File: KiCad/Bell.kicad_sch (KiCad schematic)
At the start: 34 parts, among them J1 USB-C, J2 POWER, J3 Conn_01x10, U1 ESP32-WROOM-32, U2 FT231XQ, U3 ISL89410, U4 ISL89410, U5 LMR16006+FB, U6 AA, U7 QR

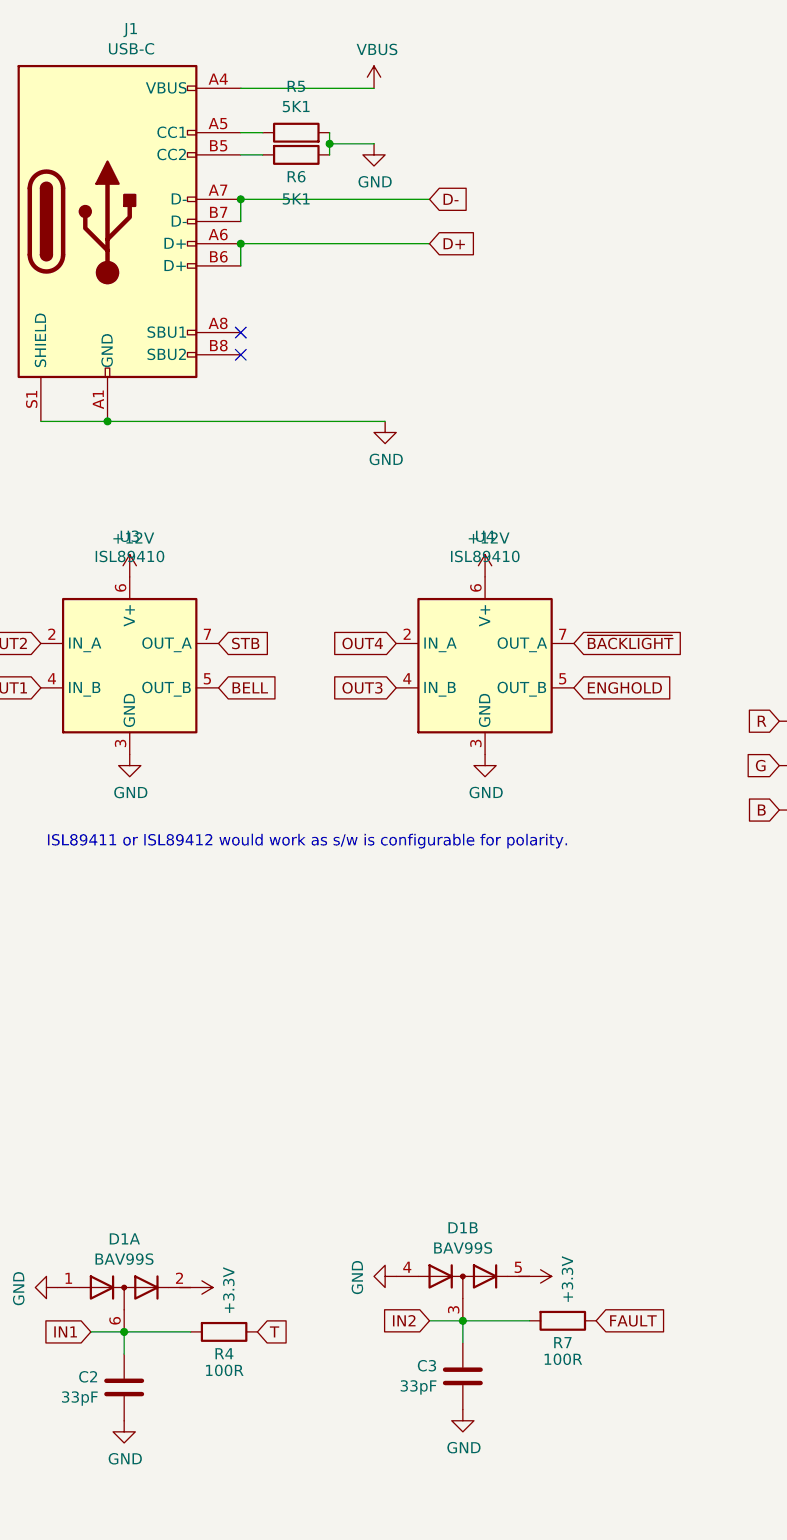
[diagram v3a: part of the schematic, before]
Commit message: VBUS update
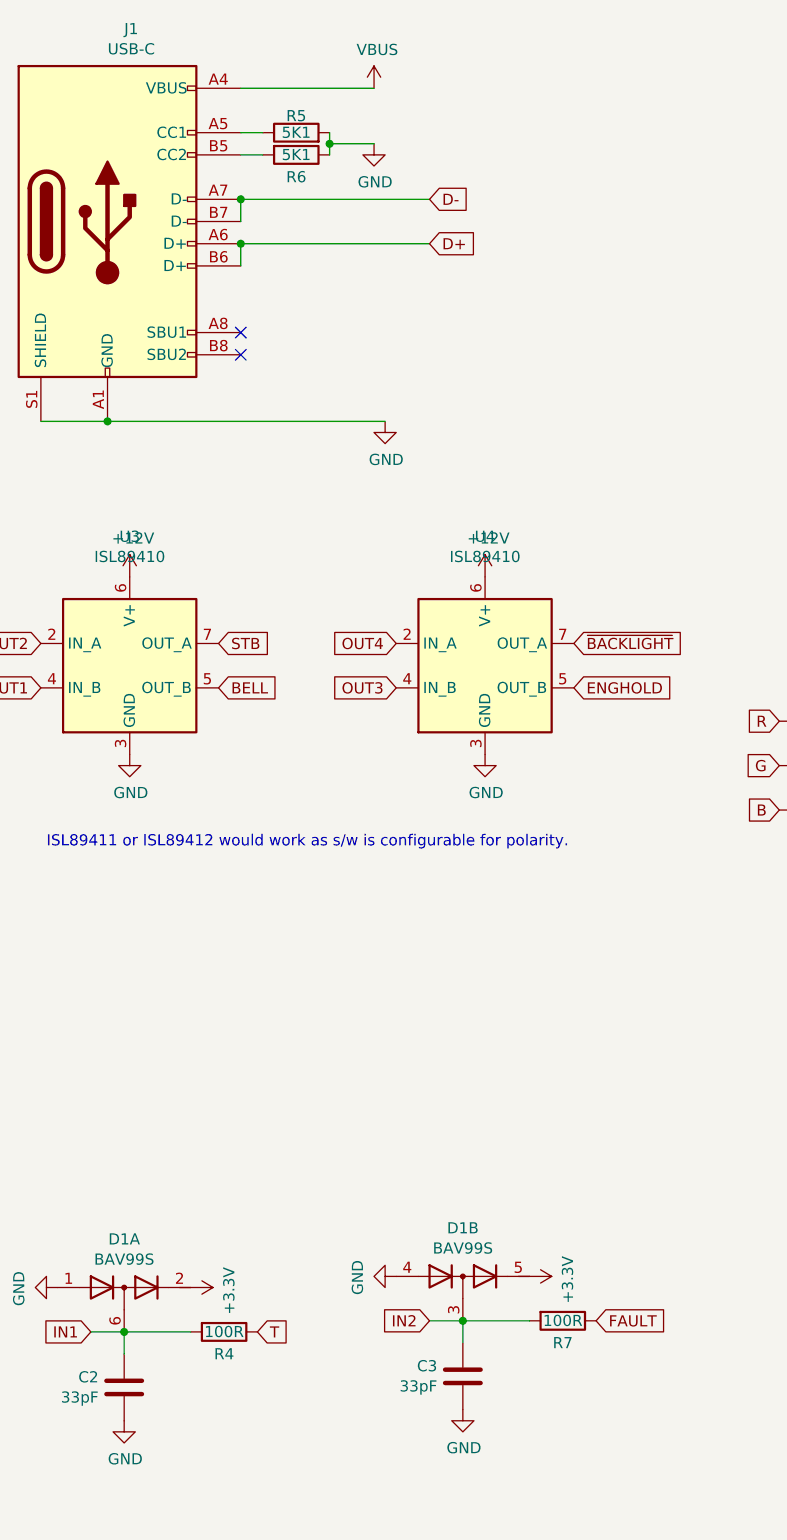
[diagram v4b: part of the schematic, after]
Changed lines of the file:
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@@
   (symbol (lib_id "Device:R") (at 132.715 27.305 90) (unit 1)
     (in_bom yes) (on_board yes)
-    (property "Reference" "R5" (id 0) (at 132.715 22.0472 90))
-    (property "Value" "5K1" (id 1) (at 132.715 24.3586 90))
+    (property "Reference" "R5" (id 0) (at 132.715 25.4 90))
+    (property "Value" "5K1" (id 1) (at 132.715 27.305 90))
     (property "Footprint" "RevK:R_0603" (id 2) (at 132.715 29.083 90)
       (effects (font (size 1.27 1.27)) hide)
@@
     (in_bom yes) (on_board yes)
     (property "Reference" "R6" (id 0) (at 132.715 32.385 90))
-    (property "Value" "5K1" (id 1) (at 132.715 34.925 90))
+    (property "Value" "5K1" (id 1) (at 132.715 29.845 90))
     (property "Footprint" "RevK:R_0603" (id 2) (at 132.715 28.067 90)
       (effects (font (size 1.27 1.27)) hide)
@@
     (in_bom yes) (on_board yes)
     (property "Reference" "R4" (id 0) (at 124.46 167.005 90))
-    (property "Value" "100R" (id 1) (at 124.46 168.91 90))
+    (property "Value" "100R" (id 1) (at 124.46 164.465 90))
     (property "Footprint" "RevK:R_0603" (id 2) (at 124.46 162.687 90)
       (effects (font (size 1.27 1.27)) hide)
@@
     (in_bom yes) (on_board yes)
     (property "Reference" "R7" (id 0) (at 163.195 165.735 90))
-    (property "Value" "100R" (id 1) (at 163.195 167.64 90))
+    (property "Value" "100R" (id 1) (at 163.195 163.195 90))
     (property "Footprint" "RevK:R_0603" (id 2) (at 163.195 161.417 90)
       (effects (font (size 1.27 1.27)) hide)

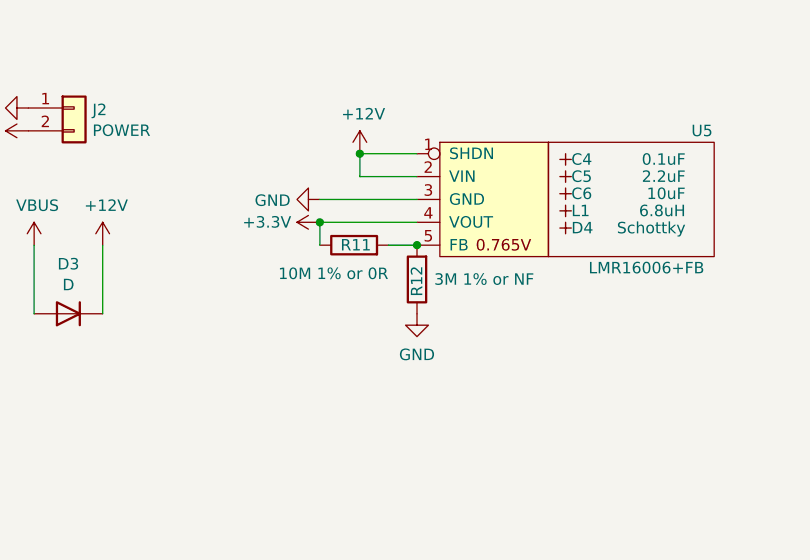
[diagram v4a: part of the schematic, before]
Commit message: Resistor fixes
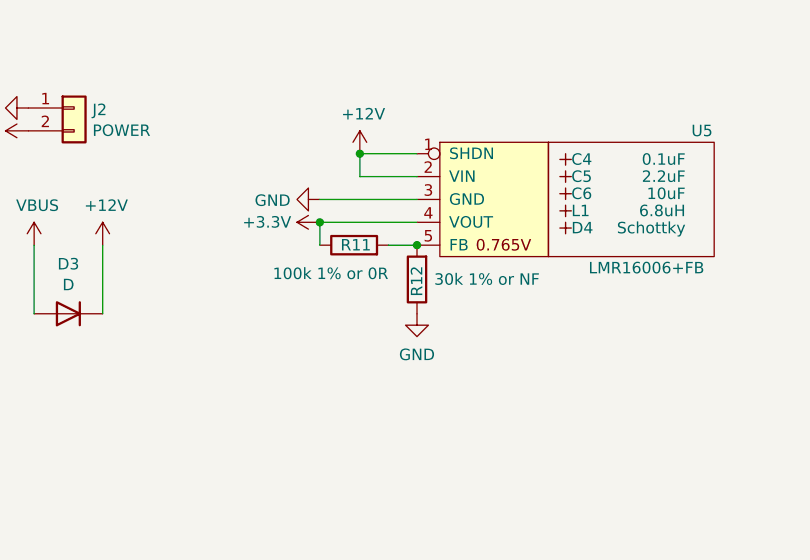
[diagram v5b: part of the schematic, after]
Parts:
- R11: value 10M 1% or 0R -> 100k 1% or 0R
- R12: value 3M 1% or NF -> 30k 1% or NF
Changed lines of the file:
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@@
       (effects (font (size 1.27 1.27)) (justify right))
     )
-    (property "Value" "3M 1% or NF" (id 1) (at 241.935 43.18 0)
+    (property "Value" "30k 1% or NF" (id 1) (at 241.935 43.18 0)
       (effects (font (size 1.27 1.27)) (justify right))
     )
@@
       (effects (font (size 1.27 1.27)) (justify left))
     )
-    (property "Value" "10M 1% or 0R" (id 1) (at 236.855 42.545 90)
+    (property "Value" "100k 1% or 0R" (id 1) (at 236.855 42.545 90)
       (effects (font (size 1.27 1.27)) (justify left))
     )
@@
     )
     (path "/c1897ab9-a710-4f2b-b18b-f2f520d0a247"
-      (reference "R11") (unit 1) (value "10M 1% or 0R") (footprint "RevK:R_0603")
+      (reference "R11") (unit 1) (value "100k 1% or 0R") (footprint "RevK:R_0603")
     )
     (path "/4c9702ac-39af-41d5-9cb6-89cc85efc703"
-      (reference "R12") (unit 1) (value "3M 1% or NF") (footprint "RevK:R_0603")
+      (reference "R12") (unit 1) (value "30k 1% or NF") (footprint "RevK:R_0603")
     )
     (path "/60e87dc7-656f-4705-b8d6-ece6cbaf41c3"
